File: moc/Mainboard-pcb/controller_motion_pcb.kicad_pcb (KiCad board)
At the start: 4 copper layers, 113 x 54 mm, 24 parts, among them J1 Conn_01x14_Male, J3 Conn_01x15_Male, P0 Conn_01x03, P1 Conn_01x03, P2 Conn_01x03, P3 Conn_01x03, P4 Conn_01x03, P5 Conn_01x03, P6 Conn_01x03, P7 Conn_01x03

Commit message: first commit
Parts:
- removed BtnMx1: Conn_02x09_Counter_Clockwise, Connector_IDC:IDC-Header_2x10_P2.54mm_Vertical
- removed CTR1: Teensy4.1, teensy:Teensy41_my
- removed ENC0, ENC1, ENC2, ENC3: Conn_01x05, Connector_JST:JST_EH_B5B-EH-A_1x05_P2.50mm_Vertical
- removed P0, P1, P2, P3, P4, P5, P6, P7: Conn_01x03, Connector_JST:JST_EH_B3B-EH-A_1x03_P2.50mm_Vertical
- removed REF** (x4): MountingHole_3.2mm_M3_Pad_Via, MountingHole:MountingHole_3.2mm_M3_Pad_Via
- removed mux1, mux2, mux3, mux4: 74HC4051, Package_DIP:DIP-16_W7.62mm
- added C1: 100nF, Capacitor_THT:C_Disc_D7.0mm_W2.5mm_P5.00mm, F.Cu at (68.5, 77.5)
- added C2: 22pF, Capacitor_THT:C_Disc_D7.0mm_W2.5mm_P5.00mm, F.Cu at (59.5, 77.5)
- added C3: 22pF, Capacitor_THT:C_Disc_D7.0mm_W2.5mm_P5.00mm, F.Cu at (54.5, 77.5)
- added C4: 10uH, Capacitor_THT:CP_Radial_D5.0mm_P2.00mm, F.Cu at (70.0, 73.0)
- added C5: 100nF, Capacitor_THT:C_Disc_D7.0mm_W2.5mm_P5.00mm, F.Cu at (71.0, 52.0)
- added C6: 100nF, Capacitor_THT:C_Disc_D7.0mm_W2.5mm_P5.00mm, B.Cu at (95.0, 67.5)
- added C7: 100nF, Capacitor_THT:C_Disc_D7.0mm_W2.5mm_P5.00mm, B.Cu at (95.0, 57.5)
- added C8: 100nF, Capacitor_THT:C_Disc_D7.0mm_W2.5mm_P5.00mm, B.Cu at (134.0, 74.0)
- added C9: 100nF, Capacitor_THT:C_Disc_D7.0mm_W2.5mm_P5.00mm, B.Cu at (199.0, 74.0)
- added J2: I2C INTERFACE MSTR, Connector_PinHeader_2.54mm:PinHeader_1x05_P2.54mm_Horizontal, F.Cu at (34.0, 54.0)
- added J4: Conn_01x02_Male, Connector_PinHeader_2.54mm:PinHeader_1x02_P2.54mm_Horizontal, B.Cu at (170.0, 55.0)
- added J5: Conn_01x02_Female, Connector_PinSocket_2.54mm:PinSocket_1x02_P2.54mm_Horizontal, B.Cu at (170.0, 69.0)
- added J6: Conn_01x06_Female, Connector_JST:JST_PH_B5B-PH-K_1x05_P2.00mm_Vertical, B.Cu at (41.0, 62.0)
- added L1: 10uH, Inductor_THT:L_Axial_L7.0mm_D3.3mm_P10.16mm_Horizontal_Fastron_MICC, F.Cu at (59.0, 55.0)
- added R1: 0, Resistor_THT:R_Axial_DIN0207_L6.3mm_D2.5mm_P10.16mm_Horizontal, F.Cu at (105.0, 68.0)
- added R10: 165, Resistor_THT:R_Axial_DIN0207_L6.3mm_D2.5mm_P10.16mm_Horizontal, B.Cu at (158.0, 57.0)
- added R11: 155, Resistor_THT:R_Axial_DIN0207_L6.3mm_D2.5mm_P10.16mm_Horizontal, B.Cu at (158.0, 53.0)
- added R12: 100, Resistor_THT:R_Axial_DIN0207_L6.3mm_D2.5mm_P10.16mm_Horizontal, B.Cu at (157.0, 73.0)
- added R13: 165, Resistor_THT:R_Axial_DIN0207_L6.3mm_D2.5mm_P10.16mm_Horizontal, B.Cu at (183.0, 57.0)
- added R14: 155, Resistor_THT:R_Axial_DIN0207_L6.3mm_D2.5mm_P10.16mm_Horizontal, B.Cu at (186.0, 54.0)
- added R15: 100, Resistor_THT:R_Axial_DIN0207_L6.3mm_D2.5mm_P10.16mm_Horizontal, B.Cu at (195.0, 74.2)
- added R16: 165, Resistor_THT:R_Axial_DIN0207_L6.3mm_D2.5mm_P10.16mm_Horizontal, B.Cu at (208.0, 57.0)
- added R17: 155, Resistor_THT:R_Axial_DIN0207_L6.3mm_D2.5mm_P10.16mm_Horizontal, B.Cu at (211.0, 57.0)
- added R18: 100, Resistor_THT:R_Axial_DIN0207_L6.3mm_D2.5mm_P10.16mm_Horizontal, B.Cu at (221.0, 74.0)
- added R19: 27k, Resistor_THT:R_Axial_DIN0207_L6.3mm_D2.5mm_P10.16mm_Horizontal, B.Cu at (95.0, 76.0)
- added R20: 27k, Resistor_THT:R_Axial_DIN0207_L6.3mm_D2.5mm_P10.16mm_Horizontal, B.Cu at (95.0, 54.0)
- added R21: 4.7k, Resistor_THT:R_Axial_DIN0207_L6.3mm_D2.5mm_P10.16mm_Horizontal, F.Cu at (71.0, 55.0)
- added R22: 10k, Resistor_THT:R_Axial_DIN0207_L6.3mm_D2.5mm_P10.16mm_Horizontal, B.Cu at (130.0, 62.0)
- added R23: 10k, Resistor_THT:R_Axial_DIN0207_L6.3mm_D2.5mm_P10.16mm_Horizontal, B.Cu at (200.0, 54.0)
- added R3: 4.7k, Resistor_THT:R_Axial_DIN0207_L6.3mm_D2.5mm_P10.16mm_Horizontal, B.Cu at (109.0, 65.0)
- added R4: 4.7k, Resistor_THT:R_Axial_DIN0207_L6.3mm_D2.5mm_P10.16mm_Horizontal, B.Cu at (145.0, 53.0)
- added R5: 4.7k, Resistor_THT:R_Axial_DIN0207_L6.3mm_D2.5mm_P10.16mm_Horizontal, B.Cu at (176.0, 56.0)
- added R6: 4.7k, Resistor_THT:R_Axial_DIN0207_L6.3mm_D2.5mm_P10.16mm_Horizontal, B.Cu at (225.0, 53.0)
- added R7: 165, Resistor_THT:R_Axial_DIN0207_L6.3mm_D2.5mm_P10.16mm_Horizontal, B.Cu at (120.0, 58.0)
- added R8: 155, Resistor_THT:R_Axial_DIN0207_L6.3mm_D2.5mm_P10.16mm_Horizontal, B.Cu at (117.0, 55.0)
- added R9: 100, Resistor_THT:R_Axial_DIN0207_L6.3mm_D2.5mm_P10.16mm_Horizontal, B.Cu at (114.0, 72.0)
- added S1: 228CMVARGBFR, flex-Ambisonic:228CMVARGBFR, F.Cu at (121.0, 65.0)
- added S2: 228CMVARGBFR, flex-Ambisonic:228CMVARGBFR, F.Cu at (153.0, 65.0)
- added S3: 228CMVARGBFR, flex-Ambisonic:228CMVARGBFR, F.Cu at (185.0, 65.0)
- added S4: 228CMVARGBFR, flex-Ambisonic:228CMVARGBFR, F.Cu at (217.0, 65.0)
- added SW1: Rotary_Encoder_Switch, MOUSERfootprintANDsymbol:PEC11R4230KS0024, F.Cu at (83.0, 67.5)
- added U1: ATtiny861V-10SU, Package_SO:SOIC-20W_7.5x12.8mm_P1.27mm, B.Cu at (59.5, 63.5)
- added U2: TPIC6C595-SOIC, Package_SO:SOIC-16_3.9x9.9mm_P1.27mm, B.Cu at (137.0, 65.0)
- added U3: TPIC6C595-SOIC, Package_SO:SOIC-16_3.9x9.9mm_P1.27mm, B.Cu at (201.0, 65.0)
- added Y1: Crystal, Crystal:Crystal_HC49-U_Vertical, F.Cu at (59.5, 73.0)
- J1: value Conn_01x14_Male -> ICSP INTERFACE; footprint Connector_PinHeader_2.54mm:PinHeader_1x14_P2.54mm_Vertical -> Connector_PinHeader_2.54mm:PinHeader_1x04_P2.54mm_Vertical; moved to B.Cu
- J3: value Conn_01x15_Male -> I2C INTERFACE SLAV; footprint Connector_PinHeader_2.54mm:PinHeader_1x15_P2.54mm_Vertical -> Connector_PinSocket_2.54mm:PinSocket_1x05_P2.54mm_Horizontal
- moved J3 108.4 mm to (34.0, 70.0), turned to 90 degrees
- moved J1 9.70 mm to (101.0, 62.9), turned to 180 degrees
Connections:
- J1 pad 1: Net-(CTR1-Pad11) -> PSHFCLK
- J1 pad 2: Net-(CTR1-Pad12) -> MISO
- J1 pad 3: Net-(CTR1-Pad13) -> MOSI
- J1 pad 4: Net-(CTR1-Pad14) -> RESET
- J3 pad 1: Net-(CTR1-Pad25) -> SDA
- J3 pad 2: Net-(CTR1-Pad26) -> GND
- J3 pad 3: Net-(CTR1-Pad27) -> SCL
- J3 pad 4: Net-(CTR1-Pad28) -> GND
- J3 pad 5: Net-(CTR1-Pad29) -> ATM_VCC
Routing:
- net GND: track 0.00 -> 374.3 mm
- net ATM_VCC: track 0.00 -> 287.1 mm, vias 0 -> 1
- net PSHFCLK: track 0.00 -> 174.5 mm, vias 0 -> 3
- net PSHFUDATE: track 0.00 -> 170.5 mm, vias 0 -> 3
- net PB3: track 0.00 -> 168.8 mm
- net s0: track 135.1 -> 0.00 mm
- net s2: track 129.8 -> 0.00 mm
- net s1: track 127.5 -> 0.00 mm
- net PB2: track 0.00 -> 126.3 mm, vias 0 -> 1
- net mux_btnMx1: track 117.6 -> 0.00 mm
- net mux_btnMx2: track 95.4 -> 0.00 mm
- net PB1: track 0.00 -> 86.4 mm
- net Net-(P0-Pad1): track 81.1 -> 0.00 mm
- net MOSI: track 0.00 -> 80.1 mm
- net RESET: track 0.00 -> 75.5 mm, vias 0 -> 1
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- removed copper zone on In2.Cu, net +3V3
- removed copper zone on In1.Cu, net GND
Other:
- board size 113 x 54 mm -> 200 x 30 mm
- copper layers 4 -> 2
- net class Default: clearance 0.2 -> 0.4; trace_width 0.25 -> 0.381; via_dia 0.8 -> 1.65; via_drill 0.4 -> 0.8
- net class VCC added: clearance 0.4, trace_width 0.6, via_dia 1.65, via_drill 0.8
- rule trace_clearance: 0.2 -> 0.4
- board text removed: "AAA Motion_Ctr-0.001"

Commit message: MCU and Controller board done
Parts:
- removed C5, C6, C7, C8, C9: 100nF, Capacitor_THT:C_Disc_D7.0mm_W2.5mm_P5.00mm
- removed J4: Conn_01x02_Male, Connector_PinHeader_2.54mm:PinHeader_1x02_P2.54mm_Horizontal
- removed J5: Conn_01x02_Female, Connector_PinSocket_2.54mm:PinSocket_1x02_P2.54mm_Horizontal
- removed J6: Conn_01x06_Female, Connector_JST:JST_PH_B5B-PH-K_1x05_P2.00mm_Vertical
- removed L1: 10uH, Inductor_THT:L_Axial_L7.0mm_D3.3mm_P10.16mm_Horizontal_Fastron_MICC
- removed R1: 0, Resistor_THT:R_Axial_DIN0207_L6.3mm_D2.5mm_P10.16mm_Horizontal
- removed R19: 27k, Resistor_THT:R_Axial_DIN0207_L6.3mm_D2.5mm_P10.16mm_Horizontal
- removed R22, R23: 10k, Resistor_THT:R_Axial_DIN0207_L6.3mm_D2.5mm_P10.16mm_Horizontal
- removed R3, R4: 4.7k, Resistor_THT:R_Axial_DIN0207_L6.3mm_D2.5mm_P10.16mm_Horizontal
- removed U3: TPIC6C595-SOIC, Package_SO:SOIC-16_3.9x9.9mm_P1.27mm
- removed Y1: Crystal, Crystal:Crystal_HC49-U_Vertical
- C1: footprint Capacitor_THT:C_Disc_D7.0mm_W2.5mm_P5.00mm -> Capacitor_SMD:C_1206_3216Metric_Pad1.33x1.80mm_HandSolder
- C2: value 22pF -> 100nF; footprint Capacitor_THT:C_Disc_D7.0mm_W2.5mm_P5.00mm -> Capacitor_SMD:C_1206_3216Metric_Pad1.33x1.80mm_HandSolder
- C3: value 22pF -> 100nF; footprint Capacitor_THT:C_Disc_D7.0mm_W2.5mm_P5.00mm -> Capacitor_SMD:C_1206_3216Metric_Pad1.33x1.80mm_HandSolder; moved to B.Cu
- C4: value 10uH -> 100nF; footprint Capacitor_THT:CP_Radial_D5.0mm_P2.00mm -> Capacitor_SMD:C_1206_3216Metric_Pad1.33x1.80mm_HandSolder; moved to B.Cu
- J1: value ICSP INTERFACE -> Conn_01x09_Male; footprint Connector_PinHeader_2.54mm:PinHeader_1x04_P2.54mm_Vertical -> Connector_PinHeader_2.54mm:PinHeader_1x09_P2.54mm_Vertical
- J2: value I2C INTERFACE MSTR -> Conn_01x09_Male; footprint Connector_PinHeader_2.54mm:PinHeader_1x05_P2.54mm_Horizontal -> Connector_PinHeader_2.54mm:PinHeader_1x09_P2.54mm_Vertical; moved to B.Cu
- J3: value I2C INTERFACE SLAV -> Conn_01x06_Female; footprint Connector_PinSocket_2.54mm:PinSocket_1x05_P2.54mm_Horizontal -> Connector_JST:JST_PH_B5B-PH-K_1x05_P2.00mm_Vertical; moved to B.Cu
- R10, R13, R16, R7: value 165 -> 100; footprint Resistor_THT:R_Axial_DIN0207_L6.3mm_D2.5mm_P10.16mm_Horizontal -> Resistor_SMD:R_1206_3216Metric_Pad1.30x1.75mm_HandSolder
- R11, R14, R8: value 155 -> 165; footprint Resistor_THT:R_Axial_DIN0207_L6.3mm_D2.5mm_P10.16mm_Horizontal -> Resistor_SMD:R_1206_3216Metric_Pad1.30x1.75mm_HandSolder
- R12, R15, R9: value 100 -> 155; footprint Resistor_THT:R_Axial_DIN0207_L6.3mm_D2.5mm_P10.16mm_Horizontal -> Resistor_SMD:R_1206_3216Metric_Pad1.30x1.75mm_HandSolder
- R17: value 155 -> 27k; footprint Resistor_THT:R_Axial_DIN0207_L6.3mm_D2.5mm_P10.16mm_Horizontal -> Resistor_SMD:R_1206_3216Metric_Pad1.30x1.75mm_HandSolder; moved to F.Cu
- R18: value 100 -> 27k; footprint Resistor_THT:R_Axial_DIN0207_L6.3mm_D2.5mm_P10.16mm_Horizontal -> Resistor_SMD:R_1206_3216Metric_Pad1.30x1.75mm_HandSolder; moved to F.Cu
- R20: value 27k -> 10k; footprint Resistor_THT:R_Axial_DIN0207_L6.3mm_D2.5mm_P10.16mm_Horizontal -> Resistor_SMD:R_1206_3216Metric_Pad1.30x1.75mm_HandSolder
- R21: value 4.7k -> 10k; footprint Resistor_THT:R_Axial_DIN0207_L6.3mm_D2.5mm_P10.16mm_Horizontal -> Resistor_SMD:R_1206_3216Metric_Pad1.30x1.75mm_HandSolder; moved to B.Cu
- R5: value 4.7k -> 165; footprint Resistor_THT:R_Axial_DIN0207_L6.3mm_D2.5mm_P10.16mm_Horizontal -> Resistor_SMD:R_1206_3216Metric_Pad1.30x1.75mm_HandSolder
- R6: value 4.7k -> 155; footprint Resistor_THT:R_Axial_DIN0207_L6.3mm_D2.5mm_P10.16mm_Horizontal -> Resistor_SMD:R_1206_3216Metric_Pad1.30x1.75mm_HandSolder
- S1, S2, S3, S4: footprint flex-Ambisonic:228CMVARGBFR -> MOUSERfootprintANDsymbol:228CMVARGBFR
- U1: value ATtiny861V-10SU -> TPIC6C595-SOIC; footprint Package_SO:SOIC-20W_7.5x12.8mm_P1.27mm -> Package_SO:SOIC-16_3.9x9.9mm_P1.27mm
- moved R17 140.5 mm to (75.5, 94.0), turned to 90 degrees
- moved R18 135.5 mm to (87.0, 94.0), turned to 90 degrees
- moved R6 128.7 mm to (99.0, 79.0), turned to 90 degrees
- moved J2 120.2 mm to (147.7, 93.0), turned to 270 degrees
- moved C4 118.6 mm to (187.5, 89.0), turned to 0 degrees
- moved R21 114.2 mm to (183.5, 74.5), turned to 180 degrees
- moved R5 82.3 mm to (99.0, 85.0)
- moved C3 69.9 mm to (123.4, 89.0), turned to 0 degrees
- moved J1 67.3 mm to (168.0, 69.0), turned to 90 degrees
- moved U1 66.1 mm to (123.0, 82.0), turned to 0 degrees
- moved J3 60.0 mm to (93.0, 81.0), turned to 270 degrees
- moved U2 53.8 mm to (188.0, 82.0)
- moved R8 39.2 mm to (148.0, 79.0), turned to 90 degrees
- moved R14 36.8 mm to (213.0, 79.0), turned to 90 degrees
- moved R9 36.4 mm to (148.0, 85.0), turned to 270 degrees
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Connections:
- C1 pad 2: ATM_VCC -> ENCA
- C2 pad 1: GND -> ENCB
- C2 pad 2: XTAL1 -> GND
- C3 pad 1: GND -> VCC
- C3 pad 2: XTAL2 -> GND
- C4 pad 1: ATM_VCC -> VCC
- J1 pad 1: PSHFCLK -> GND
- J1 pad 2: MISO -> ADC1
- J1 pad 3: MOSI -> GND
- J1 pad 4: RESET -> ADC0
- J2 pad 1: SDA -> PB0
- J2 pad 3: SCL -> PSHFDATA
- J2 pad 4: GND -> PSHFUDATE
- J2 pad 5: ATM_VCC -> PSHFCLK
- J3 pad 1: SDA -> GND
- J3 pad 2: GND -> ADC1
- J3 pad 3: SCL -> GND
- J3 pad 4: GND -> ADC0
- J3 pad 5: ATM_VCC -> VCC
- R10 pad 2: S2_R -> S2_B
- R11 pad 2: Net-(R11-Pad2) -> S3_R
- R12 pad 2: Net-(R12-Pad2) -> S3_G
- R13 pad 2: Net-(R13-Pad2) -> S3_B
- R14 pad 2: Net-(R14-Pad2) -> S4_R
- R15 pad 2: Net-(R15-Pad2) -> S4_G
- R16 pad 2: Net-(R16-Pad2) -> S4_B
- R17 pad 1: Net-(R17-Pad1) -> ENCA
- R18 pad 1: Net-(R18-Pad1) -> ENCB
- R20 pad 1: ENCB -> Net-(R20-Pad1)
- R20 pad 2: Net-(R20-Pad2) -> VCC
- R21 pad 2: ENCSW -> VCC
- R5 pad 1: PB2 -> Net-(R5-Pad1)
- R5 pad 2: Net-(R5-Pad2) -> S1_R
- R6 pad 1: PB3 -> Net-(R6-Pad1)
- R6 pad 2: Net-(R6-Pad2) -> S1_G
- R7 pad 2: S1_R -> S1_b
- R8 pad 2: S1_G -> S2_R
- R9 pad 2: S1_b -> S2_G
- S1 pad 3: Net-(R3-Pad2) -> PB0
- S1 pad 5: Net-(R9-Pad1) -> Net-(R7-Pad1)
- S1 pad 6: Net-(R7-Pad1) -> Net-(R5-Pad1)
- S1 pad 7: ATM_VCC -> VCC
- S1 pad 8: Net-(R8-Pad1) -> Net-(R6-Pad1)
- S2 pad 3: Net-(R4-Pad2) -> PB1
- S2 pad 5: Net-(R12-Pad1) -> Net-(R10-Pad1)
- S2 pad 6: Net-(R10-Pad1) -> Net-(R8-Pad1)
- S2 pad 7: ATM_VCC -> VCC
- S2 pad 8: Net-(R11-Pad1) -> Net-(R9-Pad1)
- S3 pad 3: Net-(R5-Pad2) -> PB2
- S3 pad 5: Net-(R15-Pad1) -> Net-(R13-Pad1)
- S3 pad 6: Net-(R13-Pad1) -> Net-(R11-Pad1)
- S3 pad 7: ATM_VCC -> VCC
- S3 pad 8: Net-(R14-Pad1) -> Net-(R12-Pad1)
- S4 pad 4: Net-(R6-Pad2) -> PB3
- S4 pad 5: Net-(R18-Pad1) -> Net-(R16-Pad1)
- S4 pad 6: Net-(R16-Pad1) -> Net-(R14-Pad1)
- S4 pad 7: ATM_VCC -> VCC
- S4 pad 8: Net-(R17-Pad1) -> Net-(R15-Pad1)
- SW1 pad A: Net-(R19-Pad2) -> Net-(R17-Pad2)
- SW1 pad B: Net-(R20-Pad2) -> Net-(R18-Pad2)
- SW1 pad S2: Net-(R21-Pad1) -> ENCSW
- U1 pad 1: MOSI -> VCC
- U1 pad 10: RESET -> PSHFUDATE
- U1 pad 11: ADC0 -> S2_B
- U1 pad 12: ADC1 -> (no net)
- U1 pad 13: ENCSW -> S2_R
- U1 pad 14: PB2 -> S2_G
- U1 pad 15: Net-(C5-Pad2) -> PSHFCLK
- U1 pad 2: MISO -> PSHFDATA
- U1 pad 3: PSHFCLK -> S1_b
- U1 pad 4: PSHFUDATE -> S1_R
- U1 pad 5: ATM_VCC -> S1_G
- U1 pad 6: GND -> (no net)
- U1 pad 7: XTAL1 -> Net-(R20-Pad1)
- U1 pad 8: XTAL2 -> Net-(R20-Pad1)
- U1 pad 9: ENCA -> Net-(U1-Pad9)
- U2 pad 1: ATM_VCC -> VCC
- U2 pad 11: Net-(R11-Pad2) -> S4_B
- U2 pad 13: S2_R -> S4_R
- U2 pad 14: Net-(R12-Pad2) -> S4_G
- U2 pad 2: MOSI -> Net-(U1-Pad9)
- U2 pad 3: S1_b -> S3_B
- U2 pad 4: S1_G -> S3_R
- U2 pad 5: S1_R -> S3_G
- U2 pad 7: Net-(R22-Pad1) -> Net-(R21-Pad1)
- U2 pad 8: Net-(R22-Pad1) -> Net-(R21-Pad1)
- U2 pad 9: Net-(U2-Pad9) -> (no net)
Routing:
- net ATM_VCC: track 287.1 -> 0.00 mm, vias 1 -> 0
- net VCC: track 0.00 -> 285.7 mm, vias 0 -> 5
- net PB3: track 168.8 -> 44.0 mm
- net PB2: track 126.3 -> 8.44 mm, vias 1 -> 0
- net GND: track 374.3 -> 278.9 mm, vias 0 -> 5
- net ENCB: track 13.6 -> 97.8 mm
- net MOSI: track 80.1 -> 0.00 mm
- net PSHFUDATE: track 170.5 -> 90.9 mm, vias 3 -> 5
- net Net-(U1-Pad9): track 0.00 -> 75.7 mm, vias 0 -> 2
- net RESET: track 75.5 -> 0.00 mm, vias 1 -> 0
- net ADC0: track 10.8 -> 85.4 mm, vias 0 -> 2
- net ADC1: track 16.3 -> 89.6 mm
- net PB1: track 86.4 -> 17.2 mm
- net Net-(U2-Pad9): track 68.7 -> 0.00 mm, vias 2 -> 0
- net PSHFCLK: track 174.5 -> 107.9 mm
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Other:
- board size 200 x 30 mm -> 156 x 30 mm

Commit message: Plots ready
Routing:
- net GND: vias 5 -> 9
- added copper zone on B.Cu, net GND
- added copper zone on F.Cu, net GND

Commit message: first protoype
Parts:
- J1, J2: footprint Connector_PinHeader_2.54mm:PinHeader_1x09_P2.54mm_Vertical -> .Ambisonic:Header-01x09-p2.54-selfsolder
- moved J1 10.4 mm to (157.7, 68.7), turned to 180 degrees
- moved J2 10.0 mm to (157.7, 92.7), turned to 0 degrees
- moved R5 1.50 mm to (99.0, 86.5)
- moved R7 0.50 mm to (115.5, 84.0)
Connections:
- net PB0 renamed BUT0
- net PB1 renamed BUT1
- net PB2 renamed BUT2
- net PB3 renamed BUT3
- S1 pad 1: (no net) -> unconnected-(S1-Pad1)
- S1 pad 4: (no net) -> unconnected-(S1-Pad4)
- S2 pad 2: (no net) -> unconnected-(S2-Pad2)
- S2 pad 4: (no net) -> unconnected-(S2-Pad4)
- S3 pad 1: (no net) -> unconnected-(S3-Pad1)
- S3 pad 4: (no net) -> unconnected-(S3-Pad4)
- S4 pad 2: (no net) -> unconnected-(S4-Pad2)
- S4 pad 3: (no net) -> unconnected-(S4-Pad3)
- U1 pad 12: (no net) -> unconnected-(U1-Pad12)
- U1 pad 6: (no net) -> unconnected-(U1-Pad6)
- U2 pad 12: (no net) -> unconnected-(U2-Pad12)
- U2 pad 6: (no net) -> unconnected-(U2-Pad6)
- U2 pad 9: (no net) -> unconnected-(U2-Pad9)
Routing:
- net VCC: track 285.7 -> 237.9 mm, vias 5 -> 8
- net GND: track 278.9 -> 318.2 mm, vias 9 -> 12
- net PSHFCLK: track 107.9 -> 89.6 mm, vias 3 -> 2
- net ENCB: track 97.8 -> 109.3 mm
- net Net-(R8-Pad1): track 8.51 -> 17.4 mm
- net Net-(R18-Pad2): track 4.72 -> 12.7 mm, vias 0 -> 1
- net PSHFUDATE: track 90.9 -> 98.2 mm, vias 5 -> 4
- net ENCA: track 101.5 -> 108.6 mm
- net Net-(R17-Pad2): track 4.22 -> 9.26 mm, vias 0 -> 1
- net ADC0: track 85.4 -> 90.2 mm
- net S1_G: track 23.1 -> 27.2 mm
- net BUT0: track 46.1 -> 49.8 mm
- net ADC1: track 89.6 -> 93.2 mm, vias 0 -> 1
- net S1_R: track 24.3 -> 27.8 mm
- net Net-(R5-Pad1): track 8.84 -> 5.77 mm
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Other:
- net class Default removed
- net class VCC removed

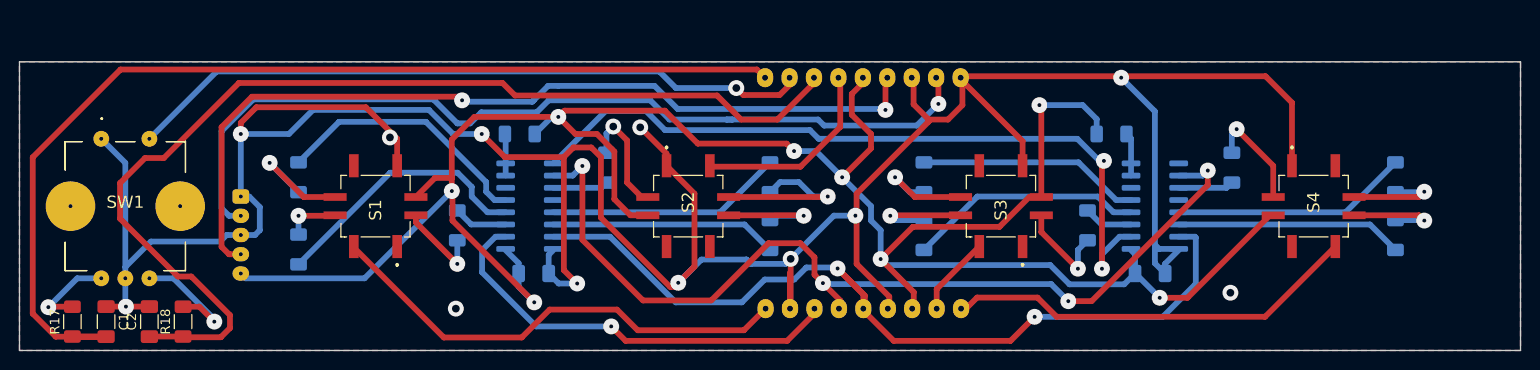
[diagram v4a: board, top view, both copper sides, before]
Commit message: split PCB Board
That's the final version for the split PCB board with 3 PCB Boards
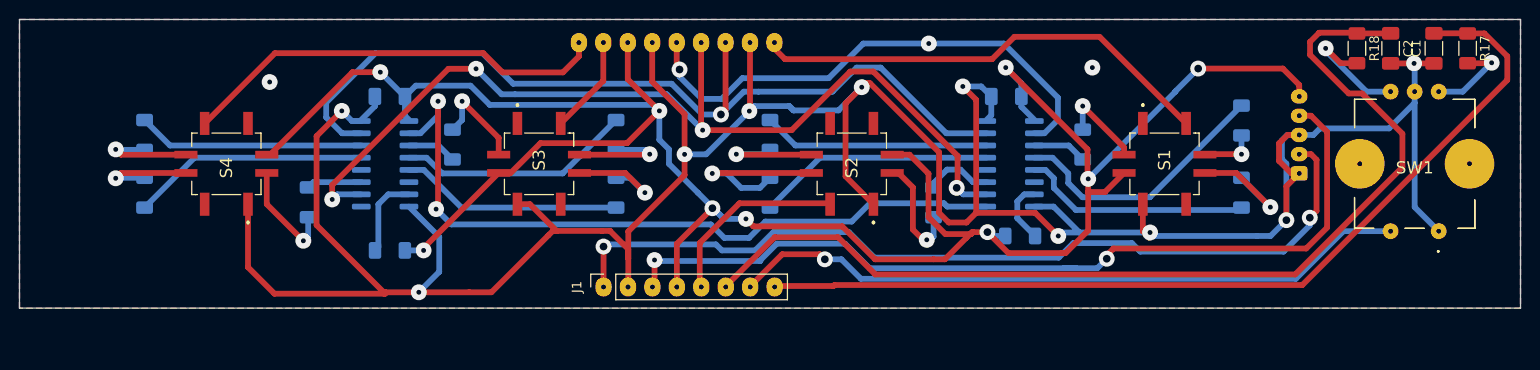
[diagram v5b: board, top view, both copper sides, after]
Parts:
- J1: value Conn_01x09_Male -> Conn_01x08_Female; footprint .Ambisonic:Header-01x09-p2.54-selfsolder -> Connector_PinSocket_2.54mm:PinSocket_1x08_P2.54mm_Vertical; moved to F.Cu
- R20, R21: value 10k -> 4K7
- moved R17 147.8 mm to (220.5, 65.6), turned to -90 degrees
- moved C1 140.9 mm to (217.0, 65.6), turned to 90 degrees
- moved SW1 139.1 mm to (217.5, 77.6), turned to 180 degrees
- moved C2 132.1 mm to (212.5, 65.6), turned to -90 degrees
- moved R15 130.4 mm to (83.0, 74.6), turned to 90 degrees
- moved R14 130.0 mm to (83.0, 80.6), turned to -90 degrees
- moved R18 125.3 mm to (209.0, 65.6), turned to -90 degrees
- moved S4 113.1 mm to (91.5, 77.6), turned to -90 degrees
- moved J3 110.0 mm to (203.0, 78.6), turned to 90 degrees
- moved R5 98.9 mm to (197.0, 73.1), turned to 90 degrees
- moved R6 98.0 mm to (197.0, 80.6), turned to -90 degrees
- moved R16 96.1 mm to (100.0, 81.6), turned to 90 degrees
- moved S1 82.1 mm to (189.0, 77.6), turned to 90 degrees
- moved C4 81.1 mm to (108.5, 70.6), turned to 180 degrees
- moved U2 80.1 mm to (108.0, 77.6), turned to 180 degrees
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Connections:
- J1 pad 1: GND -> ADC1
- J1 pad 2: ADC1 -> GND
- J1 pad 3: GND -> ADC0
- J1 pad 4: ADC0 -> VCC
- J1 pad 5: VCC -> BUT1
- J1 pad 6: BUT1 -> ENCB
- J1 pad 7: ENCB -> ENCSW
- J1 pad 8: ENCSW -> ENCA
- J2 pad 3: PSHFDATA -> PSHFCLK
- J2 pad 5: PSHFCLK -> PSHFDATA
- U1 pad 8: Net-(R20-Pad1) -> GND
- U2 pad 8: Net-(R21-Pad1) -> GND
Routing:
- net ENCA: track 108.6 -> 96.1 mm
- net PSHFDATA: track 44.2 -> 54.0 mm, vias 1 -> 2
- net GND: track 318.2 -> 314.1 mm
- net ENCB: track 109.3 -> 105.2 mm
- net Net-(R21-Pad1): track 4.52 -> 8.54 mm
- net S1_G: track 27.2 -> 23.9 mm
- net VCC: track 237.9 -> 235.1 mm, vias 8 -> 9
- net ADC1: track 93.2 -> 91.0 mm, vias 1 -> 2
- net PSHFCLK: track 89.6 -> 91.8 mm, vias 2 -> 1
- net Net-(R20-Pad1): track 4.36 -> 6.44 mm
- net BUT0: track 49.8 -> 47.9 mm
- net PSHFUDATE: track 98.2 -> 100.0 mm
- net ADC0: track 90.2 -> 91.8 mm
- net Net-(U1-Pad9): track 78.2 -> 76.7 mm
- net S2_B: track 5.75 -> 7.10 mm
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
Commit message: hardware io funzt
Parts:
- added C5: 10uF, Capacitor_THT:CP_Radial_D4.0mm_P1.50mm, B.Cu at (149.9, 101.5)
- added C6: 100nF, Capacitor_SMD:C_1206_3216Metric_Pad1.33x1.80mm_HandSolder, F.Cu at (151.3, 96.1)
- added J4: UPDI_Interface, Connector_PinHeader_2.54mm:PinHeader_1x03_P2.54mm_Vertical, B.Cu at (161.7, 48.7)
- added J5: Programm_Jumper, Connector_PinHeader_2.54mm:PinHeader_2x02_P2.54mm_Vertical, B.Cu at (160.2, 55.0)
- added REF**: thermal_via, .Ambisonic:thermal_via, F.Cu at (154.0, 95.9)
- added REF**: thermal_via, .Ambisonic:thermal_via, F.Cu at (154.6, 154.5)
- added REF**: thermal_via, .Ambisonic:thermal_via, F.Cu at (152.0, 30.3)
- added REF**: thermal_via, .Ambisonic:thermal_via, F.Cu at (157.0, 118.7)
- added REF**: thermal_via, .Ambisonic:thermal_via, F.Cu at (161.2, 46.1)
- added REF**: thermal_via, .Ambisonic:thermal_via, F.Cu at (144.2, 100.2)
- added REF**: thermal_via, .Ambisonic:thermal_via, F.Cu at (156.3, 47.4)
- added REF**: thermal_via, .Ambisonic:thermal_via, F.Cu at (143.9, 127.4)
- added REF**: thermal_via, .Ambisonic:thermal_via, F.Cu at (144.0, 59.4)
- added U3: ATtiny1626, .Ambisonic:attiny1626, B.Cu at (151.0, 92.5)
- C1, C2, R17, R18: moved to B.Cu
- C3, C4, R21: moved to F.Cu
- J1: value Conn_01x08_Female -> SPI_Female; footprint Connector_PinSocket_2.54mm:PinSocket_1x08_P2.54mm_Vertical -> Connector_PinSocket_2.54mm:PinSocket_1x05_P2.54mm_Horizontal; moved to B.Cu
- J2: value Conn_01x09_Male -> SPI_Male; footprint .Ambisonic:Header-01x09-p2.54-selfsolder -> Connector_PinHeader_2.54mm:PinHeader_1x05_P2.54mm_Horizontal
- moved R17 122.8 mm to (163.1, 174.2), turned to 180 degrees
- moved C1 118.1 mm to (163.1, 170.7), turned to 0 degrees
- moved SW1 114.8 mm to (151.1, 171.2), turned to 90 degrees
- moved C2 112.1 mm to (163.1, 166.2), turned to 180 degrees
- moved R18 107.4 mm to (163.1, 162.7), turned to 180 degrees
- moved J3 94.9 mm to (149.1, 156.7), turned to 0 degrees
- moved R5 82.4 mm to (152.7, 142.6)
- moved R6 77.9 mm to (149.9, 142.6), turned to 90 degrees
- moved R14 75.5 mm to (149.7, 45.2)
- moved R15 75.4 mm to (152.5, 45.3), turned to -90 degrees
- moved S1 75.3 mm to (151.1, 142.7), turned to 0 degrees
- moved J1 69.2 mm to (156.2, 26.1), turned to 180 degrees
- moved S4 67.8 mm to (151.1, 45.2), turned to 180 degrees
- moved R7 65.8 mm to (155.1, 136.3), turned to 90 degrees
- moved C3 59.8 mm to (152.2, 126.8), turned to 90 degrees
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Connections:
- net Net-(U1-Pad9) renamed PSHFDATA2
- J1 pad 1: ADC1 -> VCC_w
- J1 pad 2: GND -> UPDI_w
- J1 pad 3: ADC0 -> SDA
- J1 pad 4: VCC -> SCL
- J1 pad 5: BUT1 -> GND
- J2 pad 1: BUT0 -> VCC_w
- J2 pad 2: GND -> UPDI_w
- J2 pad 3: PSHFCLK -> SDA
- J2 pad 4: PSHFUDATE -> SCL
- J2 pad 5: PSHFDATA -> GND
- J3 pad 1: GND -> ADC1
- J3 pad 2: ADC1 -> GND
- J3 pad 3: GND -> ADC0
- J3 pad 4: ADC0 -> GND
- S4 pad 1: GND -> unconnected-(S4-Pad1)
- S4 pad 2: unconnected-(S4-Pad2) -> GND
- S4 pad 3: unconnected-(S4-Pad3) -> BUT3
- S4 pad 4: BUT3 -> unconnected-(S4-Pad4)
- U1 pad 11: S2_B -> unconnected-(U1-Pad11)
- U1 pad 12: unconnected-(U1-Pad12) -> S2_B
- U1 pad 15: PSHFCLK -> PSFHCLK
- U2 pad 11: S4_B -> unconnected-(U2-Pad11)
- U2 pad 12: unconnected-(U2-Pad12) -> S4_B
- U2 pad 15: PSHFCLK -> PSFHCLK
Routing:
- net GND: track 314.1 -> 442.3 mm, vias 12 -> 0
- net VCC_w: track 0.00 -> 123.6 mm, vias 0 -> 2
- net PSHFCLK: track 91.8 -> 0.00 mm, vias 1 -> 0
- net SCL: track 0.00 -> 85.3 mm, vias 0 -> 3
- net PSFHCLK: track 0.00 -> 84.5 mm, vias 0 -> 2
- net SDA: track 0.00 -> 80.3 mm, vias 0 -> 3
- net UPDI_w: track 0.00 -> 49.1 mm
- net UPDI: track 0.00 -> 42.9 mm, vias 0 -> 1
- net ADC0: track 91.8 -> 71.6 mm, vias 2 -> 1
- net BUT3: track 44.2 -> 61.6 mm, vias 0 -> 1
- net ADC1: track 91.0 -> 74.4 mm, vias 2 -> 1
- net S1_R: track 27.8 -> 12.3 mm
- net BUT0: track 47.9 -> 63.2 mm, vias 0 -> 3
- net PSHFUDATE: track 100.0 -> 87.5 mm, vias 4 -> 2
- net Net-(R8-Pad1): track 17.4 -> 5.05 mm
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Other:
- board size 156 x 30 mm -> 30 x 156 mm
